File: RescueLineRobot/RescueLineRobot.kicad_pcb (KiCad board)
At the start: 2 copper layers, 80 x 110 mm, 21 parts

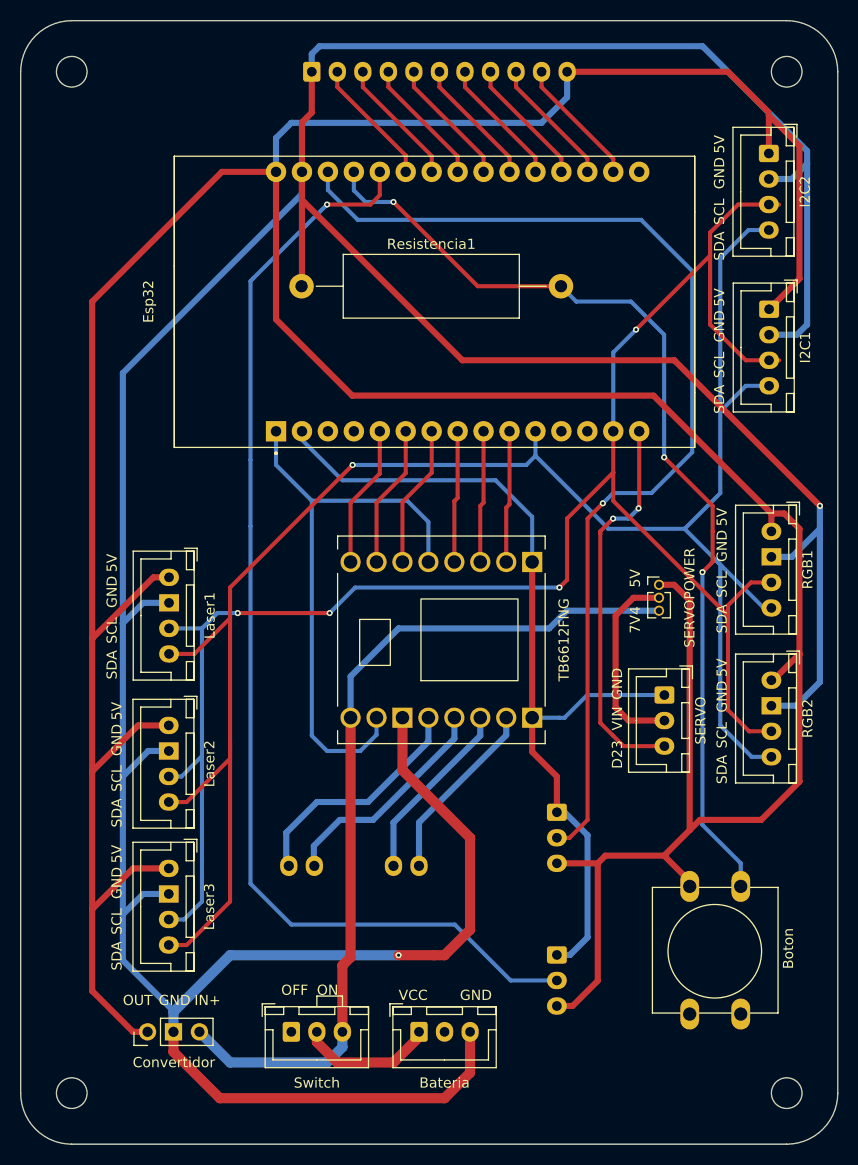
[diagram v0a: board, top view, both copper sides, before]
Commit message: Dynamis V2
- Sólo 4 i2c en la placa
- Cambiar serigrafía de los motores hacia el lado superior
- Agrandar puenteo para el voltaje del servo
- Rotar conector de QTR hacia el lado más largo de la placa
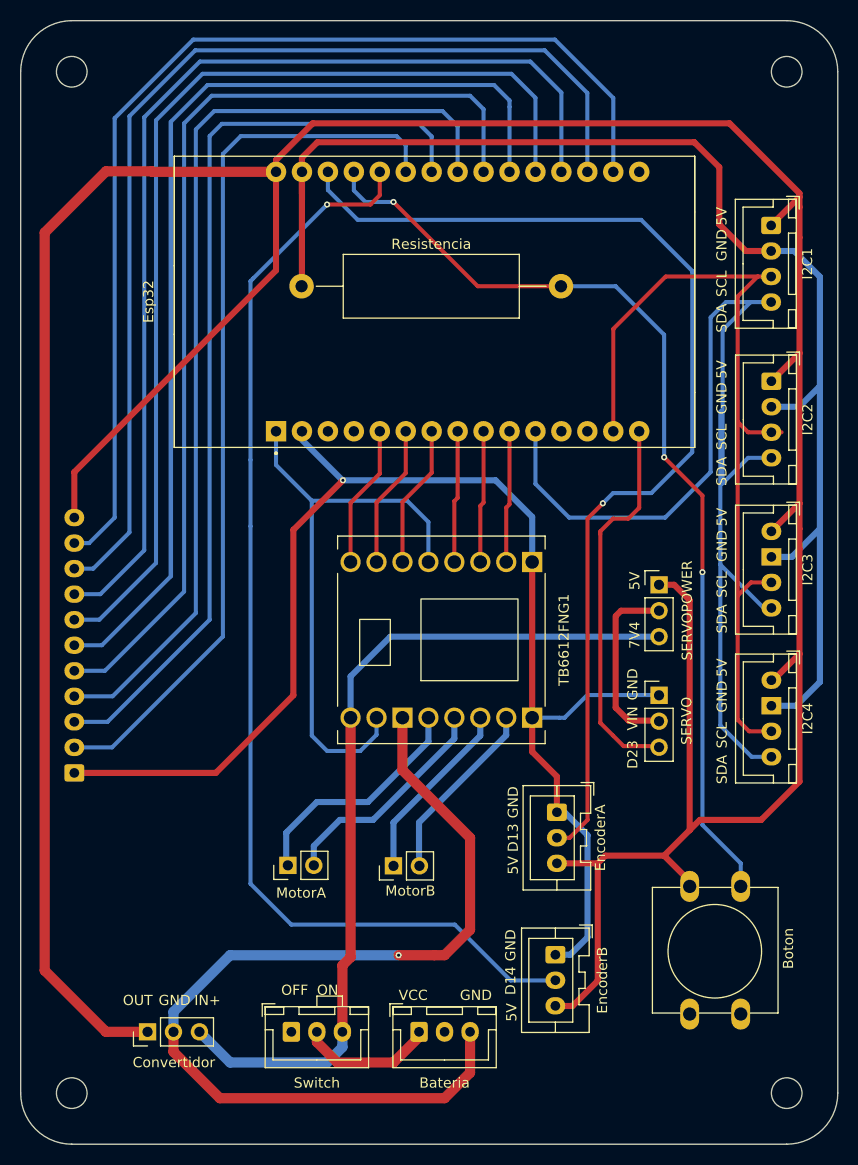
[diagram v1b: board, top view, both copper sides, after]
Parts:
- removed Laser1: Laser 1, Connector_JST:JST_XH_B4B-XH-A_1x04_P2.50mm_Vertical
- removed Laser2: Laser 2, Connector_JST:JST_XH_B4B-XH-A_1x04_P2.50mm_Vertical
- removed Laser3: Laser 3, Connector_JST:JST_XH_B4B-XH-A_1x04_P2.50mm_Vertical
- EncoderA, EncoderB: moved to F.Cu
- MotorA: renamed from MotorA1; footprint Connector_JST:JST_XH_B2B-XH-A_1x02_P2.50mm_Vertical -> Connector_PinHeader_2.54mm:PinHeader_1x02_P2.54mm_Vertical; moved to F.Cu
- MotorB: renamed from MotorB1; footprint Connector_JST:JST_XH_B2B-XH-A_1x02_P2.50mm_Vertical -> Connector_PinHeader_2.54mm:PinHeader_1x02_P2.54mm_Vertical; moved to F.Cu
- SERVO: footprint Connector_JST:JST_XH_B3B-XH-A_1x03_P2.50mm_Vertical -> Connector_PinHeader_2.54mm:PinHeader_1x03_P2.54mm_Vertical
- SERVOPOWER: footprint Connector_PinHeader_1.27mm:PinHeader_1x03_P1.27mm_Vertical -> Connector_PinHeader_2.54mm:PinHeader_1x03_P2.54mm_Vertical
- moved SigueLineas 72.5 mm to (60.2, 113.7), turned to 90 degrees
- moved I2C1 7.05 mm to (128.5, 60.0)
- moved I2C2 7.05 mm to (128.5, 75.3)
- moved SERVO 0.53 mm to (117.5, 106.0), turned to 0 degrees
- moved EncoderB 0.15 mm to (107.3, 131.4)
- moved MotorA 0.10 mm to (81.2, 122.7), turned to 90 degrees
- turned MotorB to 90 degrees
- renumbered I2C2 to I2C1, I2C1 to I2C2, RGB1 to I2C3, RGB2 to I2C4, Resistencia1 to Resistencia, TB6612FNG to TB6612FNG1
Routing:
- net GND: track 489.4 -> 367.5 mm
- net D22: track 179.1 -> 84.1 mm, vias 4 -> 0
- net D36: track 12.7 -> 105.7 mm
- net D39: track 12.7 -> 104.6 mm
- net D34: track 12.7 -> 103.1 mm
- net D35: track 12.7 -> 100.9 mm
- net D32: track 12.6 -> 99.1 mm
- net D33: track 12.6 -> 96.9 mm
- net D25: track 12.6 -> 94.1 mm
- net D26: track 12.6 -> 91.0 mm
- net D27: track 12.6 -> 87.9 mm
- net D21: track 184.4 -> 115.7 mm, vias 1 -> 0
- net 5V: track 387.5 -> 355.6 mm
- net 7V4: track 85.3 -> 84.3 mm
- net D12: track 96.0 -> 95.2 mm
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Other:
- board text added: "Dynamis Bot V2, 2026"
- board text removed: "Dynamis Bot, 2024"

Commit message: Arreglo regulador de voltaje
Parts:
- Convertidor1: renamed from Convertidor; footprint Connector_PinHeader_2.54mm:PinHeader_1x03_P2.54mm_Vertical -> Connector_PinHeader_2.54mm:PinHeader_2x03_P2.54mm_Vertical
- MotorA1: renamed from MotorA; footprint Connector_PinHeader_2.54mm:PinHeader_1x02_P2.54mm_Vertical -> Connector_JST:JST_XH_B2B-XH-A_1x02_P2.50mm_Vertical
- MotorB1: renamed from MotorB; footprint Connector_PinHeader_2.54mm:PinHeader_1x02_P2.54mm_Vertical -> Connector_JST:JST_XH_B2B-XH-A_1x02_P2.50mm_Vertical
- SERVO1: renamed from SERVO; footprint Connector_PinHeader_2.54mm:PinHeader_1x03_P2.54mm_Vertical -> Connector_JST:JST_XH_B3B-XH-A_1x03_P2.50mm_Vertical
- moved Convertidor1 10.5 mm to (66.9, 128.5)
- turned SERVO1 to -90 degrees
- renumbered Bateria to Bateria1, Boton to Boton1, EncoderA to EncoderA1, EncoderB to EncoderB1, I2C2 to I2C1, I2C1 to I2C2, I2C4 to I2C3, I2C3 to I2C4, Resistencia to Resistencia1, SERVOPOWER to SERVOPOWER1, SigueLineas to SigueLineas1, Switch to Switch1
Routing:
- net GND: track 367.5 -> 403.3 mm
- net 7V4: track 84.3 -> 95.0 mm
- net 5V: track 355.6 -> 362.1 mm

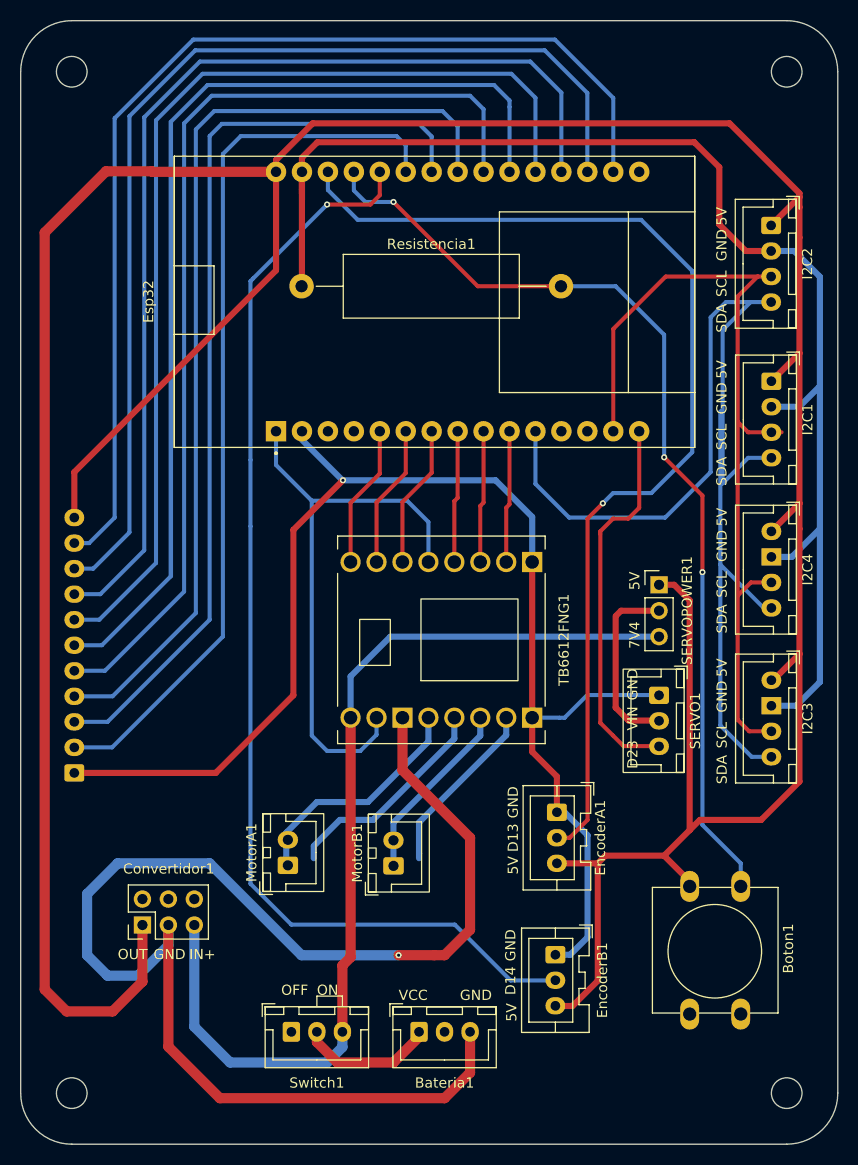
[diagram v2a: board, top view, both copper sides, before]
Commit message: Cambio giroscopio
Se cambio el sistema de acople del giroscopio para que sea igual al del conversor de voltaje
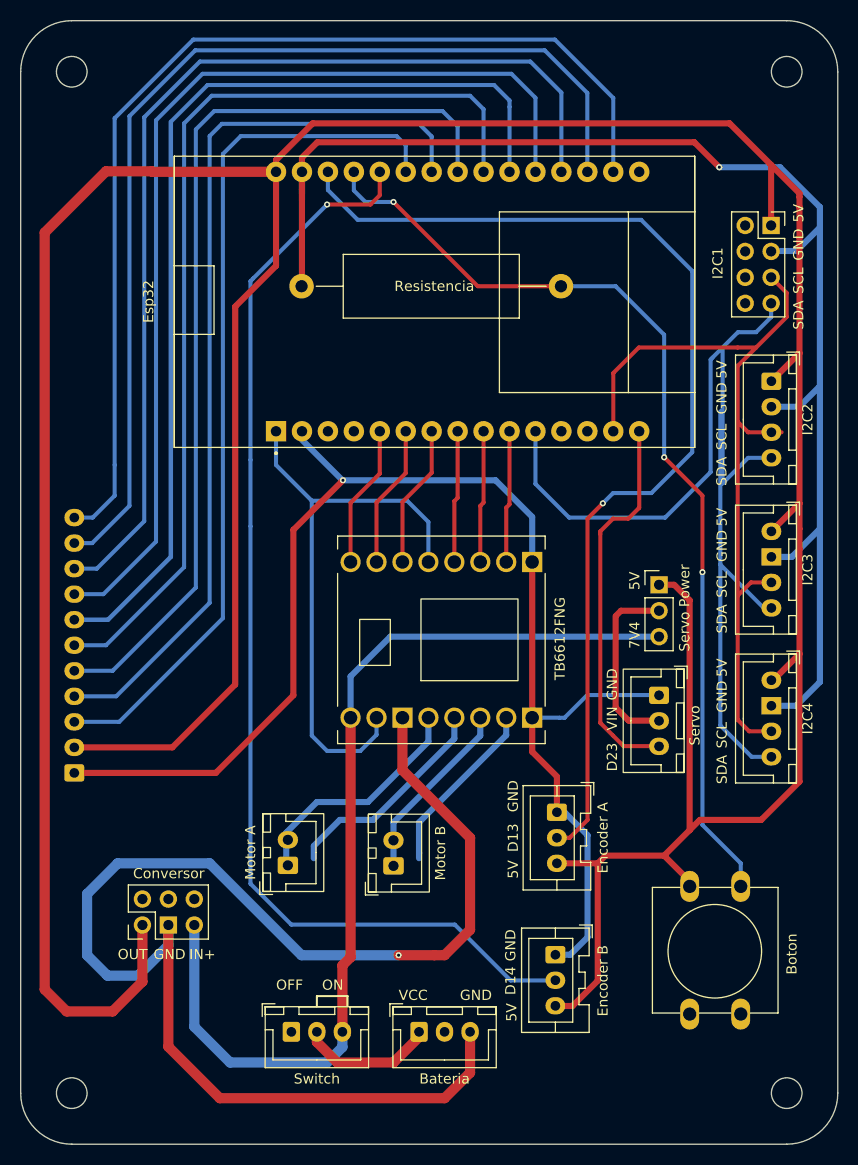
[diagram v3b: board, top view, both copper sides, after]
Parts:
- Boton1: value SW_Push -> Boton
- Convertidor1: value Convertidor -> Conversor
- I2C1: renamed from I2C2; footprint Connector_JST:JST_XH_B4B-XH-A_1x04_P2.50mm_Vertical -> Connector_PinSocket_2.54mm:PinSocket_2x04_P2.54mm_Vertical
- MotorA1: value Motor 1 -> Motor A
- MotorB1: value MotorB -> Motor B
- Resistencia1: value R -> Resistencia
- SERVO1: value Conn_01x03 -> Servo
- SERVOPOWER1: value Conn_01x03 -> Servo Power
- SigueLineas1: value Conn_01x11 -> SigueLineas
- TB6612FNG1: value ROB-14450 -> TB6612FNG
- turned I2C1 to 0 degrees
- renumbered I2C1 to I2C2, I2C4 to I2C3, I2C3 to I2C4
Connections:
- SigueLineas1 pad 10: D36 -> D39
- SigueLineas1 pad 11: 5V -> D36
- SigueLineas1 pad 2: D27 -> 5V
- SigueLineas1 pad 3: D26 -> D27
- SigueLineas1 pad 4: D25 -> D26
- SigueLineas1 pad 5: D33 -> D25
- SigueLineas1 pad 6: D32 -> D33
- SigueLineas1 pad 7: D35 -> D32
- SigueLineas1 pad 8: D34 -> D35
- SigueLineas1 pad 9: D39 -> D34
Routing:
- net 5V: track 362.1 -> 392.3 mm
- net D21: track 115.7 -> 108.5 mm
- net GND: track 403.3 -> 409.7 mm, vias 2 -> 3
- net D22: track 84.1 -> 79.0 mm
- net D34: track 103.1 -> 100.4 mm
- net D39: track 104.6 -> 102.0 mm
- net D25: track 94.1 -> 91.6 mm
- net D33: track 96.9 -> 94.5 mm
- net D36: track 105.7 -> 103.4 mm
- net D35: track 100.9 -> 98.6 mm
- net D32: track 99.1 -> 96.9 mm
- net D27: track 87.9 -> 85.8 mm
- net D26: track 91.0 -> 89.0 mm
